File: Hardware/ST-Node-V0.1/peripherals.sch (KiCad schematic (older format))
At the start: 30 parts, among them Q2 2SC4213, SW2 SW_Push, U10 LIS2DH12, U11 SHTC3, U12 ATECC608A-TNGLORAU, U9 MX25R1635

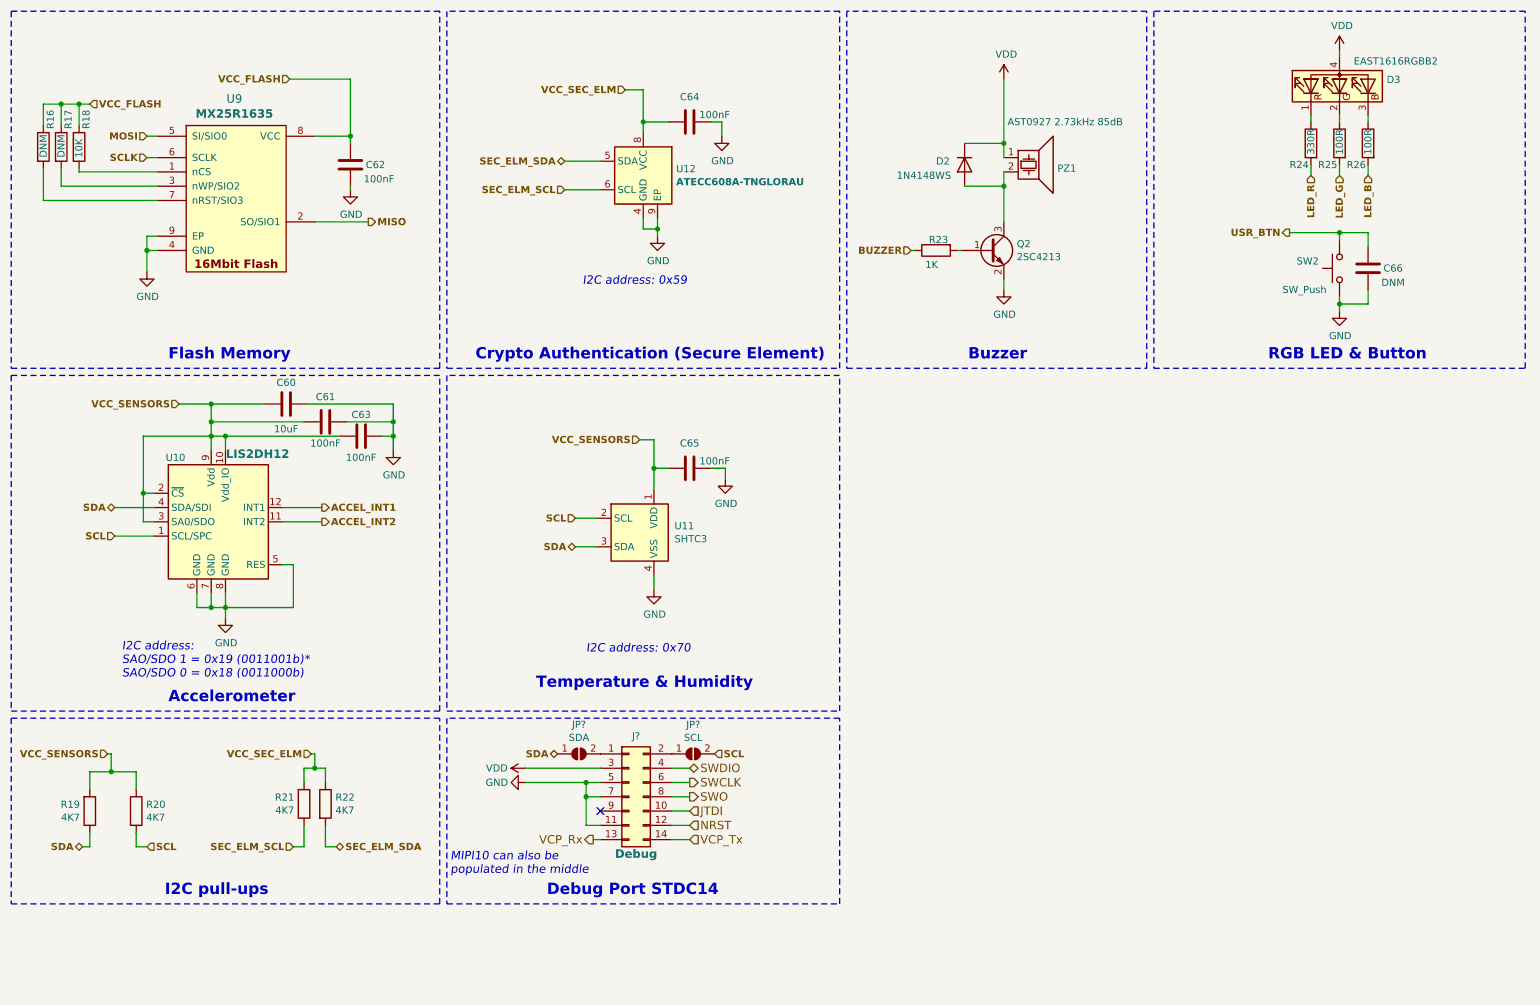
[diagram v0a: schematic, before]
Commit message: sch:  Swap couple of pins and fix a HW bug
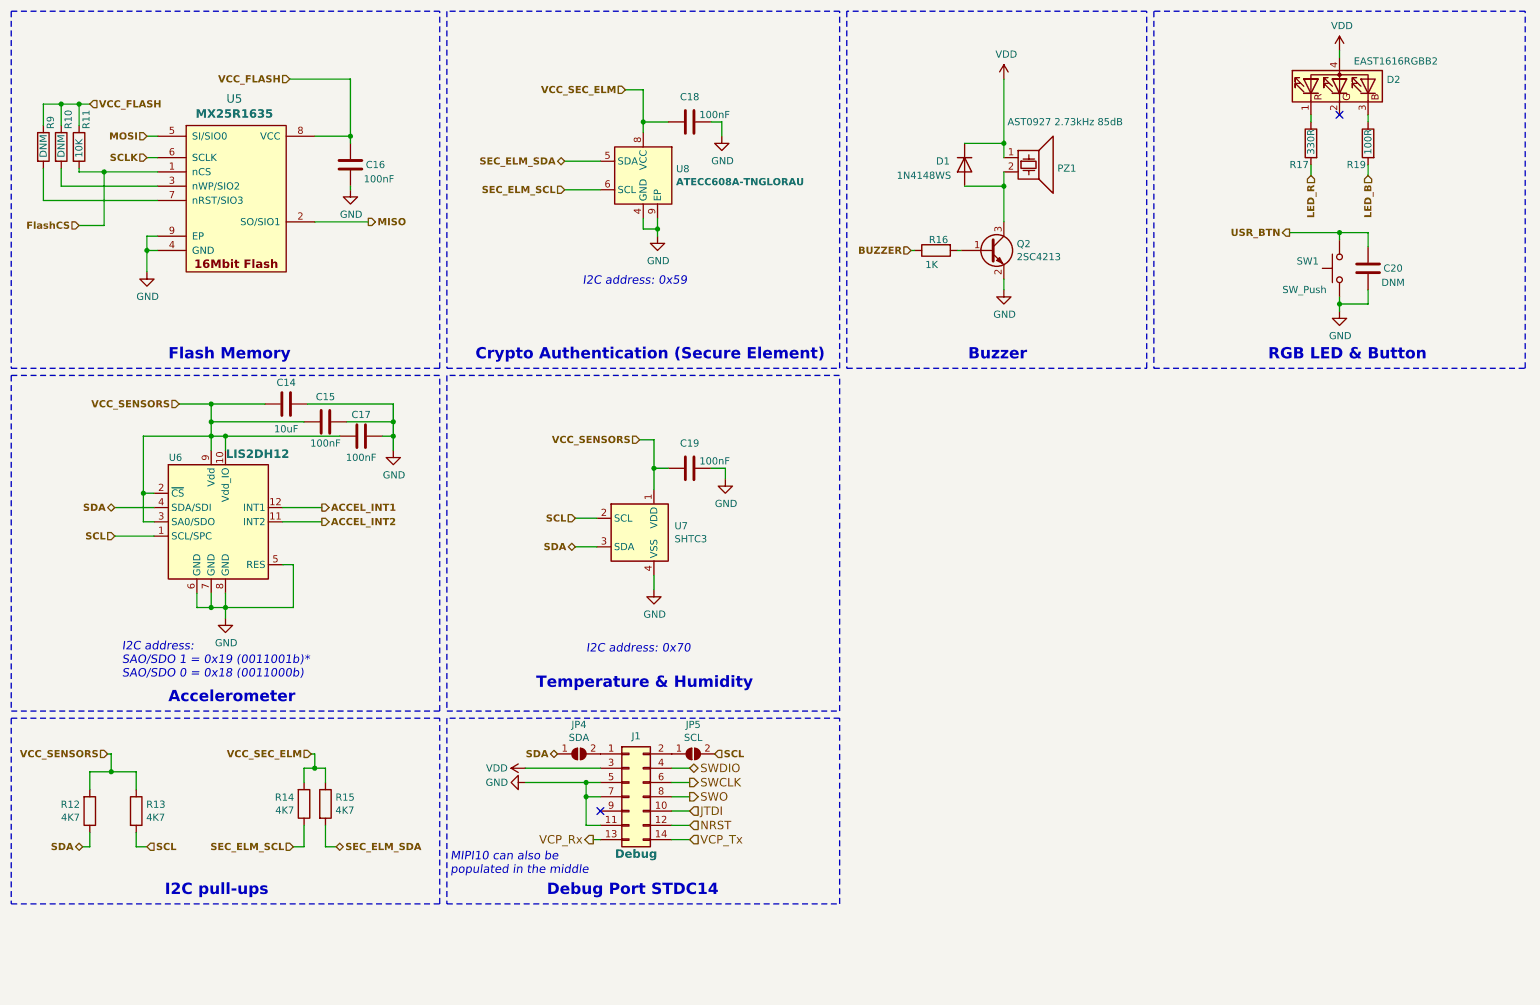
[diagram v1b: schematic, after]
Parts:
- removed R25: 100R, Resistor_SMD:R_0402_1005Metric, symbol Device:R
- J1: renamed from J?; footprint (none) -> Connector_PinHeader_1.27mm:PinHeader_2x07_P1.27mm_Vertical_SMD
- JP4, JP5: renamed from JP?; footprint (none) -> Jumper:SolderJumper-2_P1.3mm_Open_RoundedPad1.0x1.5mm
- renumbered C60 to C14, C61 to C15, C62 to C16, C63 to C17, C64 to C18, C65 to C19, C66 to C20, D2 to D1, D3 to D2, R17 to R10, R18 to R11, R19 to R12, R20 to R13, R21 to R14, R22 to R15, R23 to R16, R24 to R17, R26 to R19, R16 to R9, SW2 to SW1, U9 to U5, U10 to U6, U11 to U7, U12 to U8
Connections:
- net FlashCS: now reaches R11.2, U5.1 (nCS)
- no-connect marks 1 -> 2

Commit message: sch, pcb: Improve pcb layout, swap sch pins
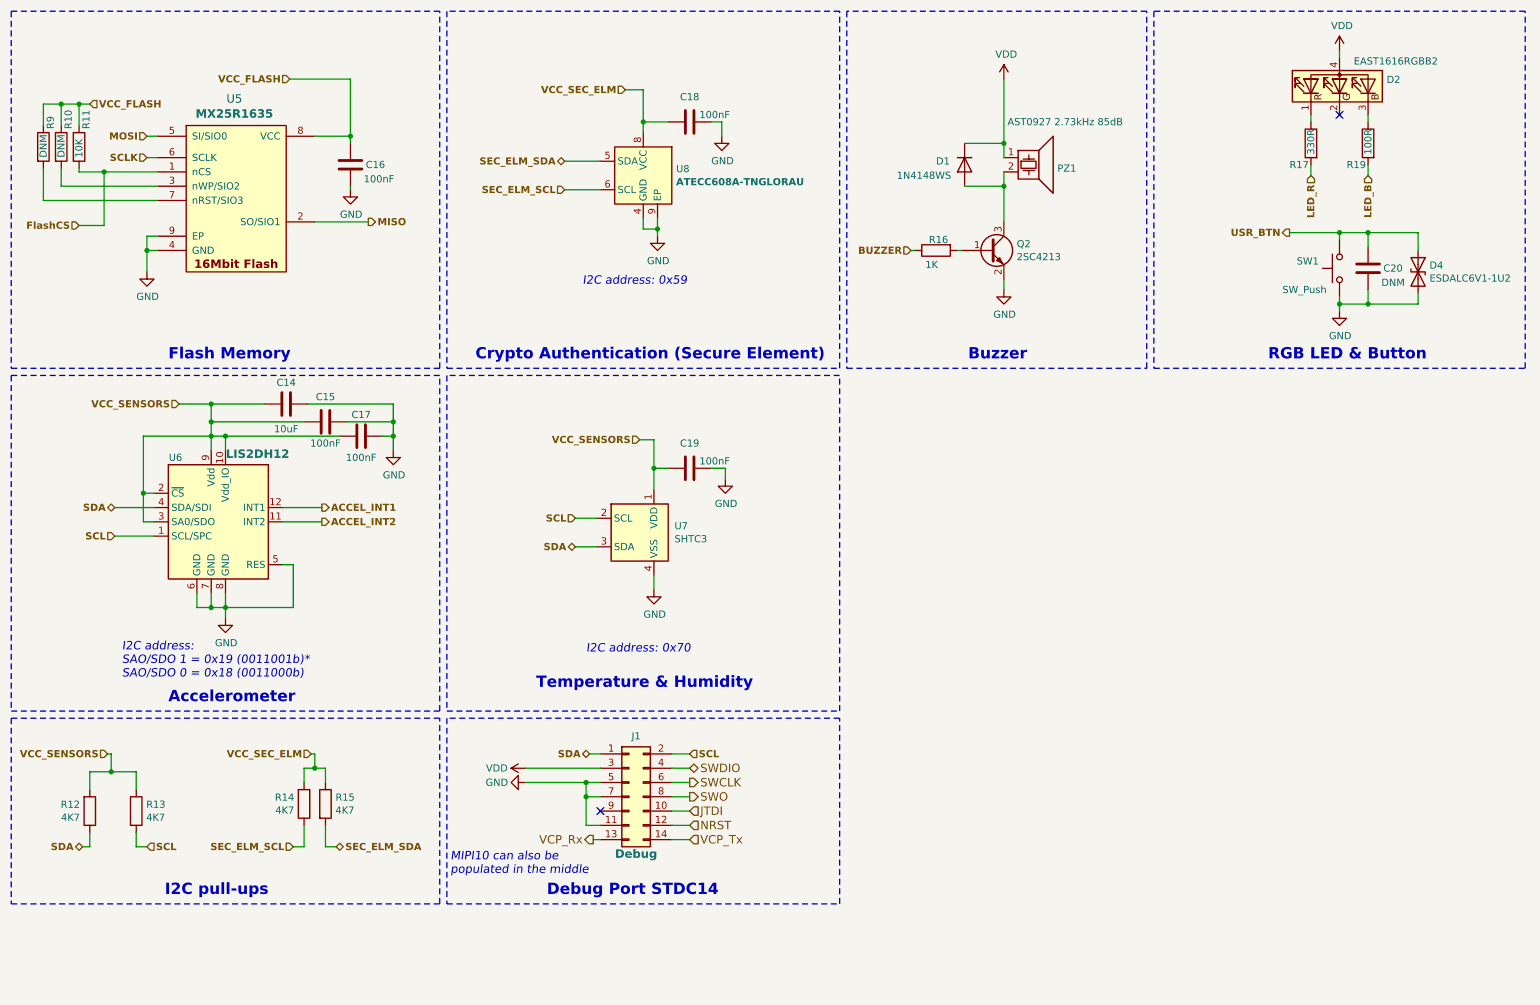
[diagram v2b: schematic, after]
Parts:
- removed JP4: SDA, Jumper:SolderJumper-2_P1.3mm_Open_RoundedPad1.0x1.5mm, symbol Jumper:SolderJumper_2_Open
- removed JP5: SCL, Jumper:SolderJumper-2_P1.3mm_Open_RoundedPad1.0x1.5mm, symbol Jumper:SolderJumper_2_Open
- added D4: ESDALC6V1-1U2, Diode_SMD:D_0201_0603Metric, symbol Device:D_TVS
- C14: MPN (none) -> C1608X5R0J106K080AB
- C15, C16, C17, C18, C19: MPN (none) -> CC0402KRX7R7BB104
- D2: footprint LED_SMD:LED_RGB_1210 -> node-lib-v1:LED_RGB_0606
- J1: footprint Connector_PinHeader_1.27mm:PinHeader_2x07_P1.27mm_Vertical_SMD -> node-lib-v1:PinHeader_2x07_P1.27mm_Vertical_SMD; MPN (none) -> FTSH-107-01-F-DV-K
- PZ1: footprint Buzzer_Beeper:MagneticBuzzer_CUI_CST-931RP-A -> node-lib-v1:Buzzer_AST0927MW-3.6TRQ
- R10, R9: MPN (none) -> DNM
- R11: MPN (none) -> AC0402JR-0710KL
- R12, R13, R14, R15: MPN (none) -> AC0402FR-074K7L
- R16: MPN (none) -> RC0402FR-071KP
- R17: MPN (none) -> AC0402FR-07330RL
- R19: MPN (none) -> RC0402FR-07100RL
- SW1: footprint Button_Switch_SMD:SW_SPST_B3S-1000 -> node-lib-v1:EVQ-P2R02W; MPN KMR211GLFS -> EVQ-P2R02W
- U5: footprint Package_CSP:LFCSP-8-1EP_3x2mm_P0.5mm_EP1.6x1.65mm -> node-lib-v1:FLASH_UFDFN-8-MX25R1635F
- U7: footprint Sensor_Humidity:Sensirion_DFN-4-1EP_2x2mm_P1mm_EP0.7x1.6mm -> node-lib-v1:Sensirion_DFN-4-1EP_2x2mm_P1mm_EP0.7x1.6mm; MPN (none) -> SHTC3
- U8: MPN ATECC608A-TNGLORAU-G -> ATECC608A-TNGLORAU-B
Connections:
- net GND: now also D4.2 (A2)
- net SCL: now also J1.2 (Pin_2)
- net SDA: now also J1.1 (Pin_1)
- net USR_BTN: now also D4.1 (A1)
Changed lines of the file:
@@
 F 0 "U5" H 2112 1687 59  0000 C CNN
 F 1 "MX25R1635" H 2112 1582 59  0000 C CNB
-F 2 "Package_CSP:LFCSP-8-1EP_3x2mm_P0.5mm_EP1.6x1.65mm" H 1775 1425 59  0001 C CNN
+F 2 "node-lib-v1:FLASH_UFDFN-8-MX25R1635F" H 1775 1425 59  0001 C CNN
 F 3 "" H 1775 1425 59  0001 C CNN
 F 4 "MX25R1635FZUIL0" H 1775 1425 50  0001 C CNN "MPN"
@@
 F 2 "Capacitor_SMD:C_0603_1608Metric" H 2513 3150 50  0001 C CNN
 F 3 "~" H 2475 3300 50  0001 C CNN
+F 4 "C1608X5R0J106K080AB" V 2475 3300 50  0001 C CNN "MPN"
 	1    2475 3300
 	0    1    1    0
@@
 F 2 "Capacitor_SMD:C_0402_1005Metric" H 2788 3275 50  0001 C CNN
 F 3 "~" H 2750 3425 50  0001 C CNN
+F 4 "CC0402KRX7R7BB104" H 2750 3425 50  0001 C CNN "MPN"
 	1    2750 3425
 	0    1    1    0
@@
 F 2 "Capacitor_SMD:C_0402_1005Metric" H 3038 3375 50  0001 C CNN
 F 3 "~" H 3000 3525 50  0001 C CNN
+F 4 "CC0402KRX7R7BB104" H 3000 3525 50  0001 C CNN "MPN"
 	1    3000 3525
 	0    1    1    0
@@
 F 2 "Capacitor_SMD:C_0402_1005Metric" H 2963 1475 50  0001 C CNN
 F 3 "~" H 2925 1625 50  0001 C CNN
+F 4 "CC0402KRX7R7BB104" H 2925 1625 50  0001 C CNN "MPN"
 	1    2925 1625
 	-1   0    0    1
@@
 	1575 1575 1500 1575
 $Comp
-L Device:R R11
-U 1 1 5EBDE849
-P 1025 1500
-F 0 "R11" V 1075 1625 50  0000 L CNN
-F 1 "10K" V 1025 1425 50  0000 L CNN
-F 2 "Resistor_SMD:R_0402_1005Metric" V 955 1500 50  0001 C CNN
-F 3 "~" H 1025 1500 50  0001 C CNN
-	1    1025 1500
-	1    0    0    -1
-$EndComp
-$Comp
 L Device:R R10
 U 1 1 5EBDF77C
@@
 F 2 "Resistor_SMD:R_0402_1005Metric" V 830 1500 50  0001 C CNN
 F 3 "~" H 900 1500 50  0001 C CNN
+F 4 "DNM" H 900 1500 50  0001 C CNN "MPN"
 	1    900  1500
 	1    0    0    -1
@@
 F 2 "Resistor_SMD:R_0402_1005Metric" V 705 1500 50  0001 C CNN
 F 3 "~" H 775 1500 50  0001 C CNN
+F 4 "DNM" H 775 1500 50  0001 C CNN "MPN"
 	1    775  1500
 	1    0    0    -1
@@
 F 2 "Capacitor_SMD:C_0402_1005Metric" H 5338 1175 50  0001 C CNN
 F 3 "~" H 5300 1325 50  0001 C CNN
+F 4 "CC0402KRX7R7BB104" H 5300 1325 50  0001 C CNN "MPN"
 	1    5300 1325
 	0    1    1    0
@@
 F 2 "Package_DFN_QFN:DFN-8-1EP_3x2mm_P0.5mm_EP1.3x1.5mm" H 4975 1700 50  0001 C CNN
 F 3 "http://ww1.microchip.com/downloads/en/DeviceDoc/ATECC608A-CryptoAuthentication-Device-Summary-Data-Sheet-DS40001977B.pdf" H 5125 1950 50  0001 C CNN
-F 4 "ATECC608A-TNGLORAU-G" H 4975 1700 50  0001 C CNN "MPN"
+F 4 "ATECC608A-TNGLORAU-B" H 4975 1700 50  0001 C CNN "MPN"
 	1    4975 1700
 	-1   0    0    -1
@@
 F 0 "PZ1" H 7875 1500 50  0000 L CNN
 F 1 "AST0927 2.73kHz 85dB" H 7525 1825 50  0000 L CNN
-F 2 "Buzzer_Beeper:MagneticBuzzer_CUI_CST-931RP-A" H 7665 1525 50  0001 C CNN
+F 2 "node-lib-v1:Buzzer_AST0927MW-3.6TRQ" H 7665 1525 50  0001 C CNN
 F 3 "~" H 7665 1525 50  0001 C CNN
 F 4 "AST0927MW-3.6TRQ" H 7700 1575 50  0001 C CNN "MPN"
@@
 F 2 "Resistor_SMD:R_0402_1005Metric" V 6955 2225 50  0001 C CNN
 F 3 "~" H 7025 2225 50  0001 C CNN
+F 4 "RC0402FR-071KP" H 7025 2225 50  0001 C CNN "MPN"
 	1    7025 2225
 	0    -1   1    0
@@
 F 0 "D2" V 9896 745 50  0000 R CNN
 F 1 "EAST1616RGBB2" V 10025 975 50  0000 R CNN
-F 2 "LED_SMD:LED_RGB_1210" H 9850 1025 50  0001 C CNN
+F 2 "node-lib-v1:LED_RGB_0606" H 9850 1025 50  0001 C CNN
 F 3 "~" H 9850 1025 50  0001 C CNN
 F 4 "EAST1616RGBB2" V 9850 1075 50  0001 C CNN "MPN"
@@
 F 2 "Resistor_SMD:R_0402_1005Metric" V 9580 1475 50  0001 C CNN
 F 3 "~" H 9650 1475 50  0001 C CNN
+F 4 "AC0402FR-07330RL" H 9650 1475 50  0001 C CNN "MPN"
 	1    9650 1475
 	-1   0    0    -1
@@
 F 2 "Resistor_SMD:R_0402_1005Metric" V 9980 1475 50  0001 C CNN
 F 3 "~" H 10050 1475 50  0001 C CNN
+F 4 "RC0402FR-07100RL" H 10050 1475 50  0001 C CNN "MPN"
 	1    10050 1475
 	-1   0    0    -1
@@
 F 0 "SW1" V 9900 2650 50  0000 R CNN
 F 1 "SW_Push" V 9700 2750 50  0000 R CNN
-F 2 "Button_Switch_SMD:SW_SPST_B3S-1000" H 9850 2550 50  0001 C CNN
+F 2 "node-lib-v1:EVQ-P2R02W" H 9850 2550 50  0001 C CNN
 F 3 "~" H 9850 2550 50  0001 C CNN
-F 4 "KMR211GLFS" H 9850 2350 50  0001 C CNN "MPN"
+F 4 "EVQ-P2R02W" H 9850 2350 50  0001 C CNN "MPN"
 	1    9850 2350
 	0    -1   -1   0
@@
 F 0 "U7" H 5194 4246 50  0000 L CNN
 F 1 "SHTC3" H 5194 4155 50  0000 L CNN
-F 2 "Sensor_Humidity:Sensirion_DFN-4-1EP_2x2mm_P1mm_EP0.7x1.6mm" H 5150 3850 50  0001 C CNN
+F 2 "node-lib-v1:Sensirion_DFN-4-1EP_2x2mm_P1mm_EP0.7x1.6mm" H 5150 3850 50  0001 C CNN
 F 3 "https://www.sensirion.com/fileadmin/user_upload/customers/sensirion/Dokumente/0_Datasheets/Humidity/Sensirion_Humidity_Sensors_SHTC3_Datasheet.pdf" H 4650 4650 50  0001 C CNN
+F 4 "SHTC3" H 4950 4200 50  0001 C CNN "MPN"
 	1    4950 4200
 	1    0    0    -1
@@
 F 2 "Capacitor_SMD:C_0402_1005Metric" H 5338 3600 50  0001 C CNN
 F 3 "~" H 5300 3750 50  0001 C CNN
+F 4 "CC0402KRX7R7BB104" H 5300 3750 50  0001 C CNN "MPN"
 	1    5300 3750
 	0    1    1    0
@@
 F 2 "Resistor_SMD:R_0402_1005Metric" V 2680 6100 50  0001 C CNN
 F 3 "~" H 2750 6100 50  0001 C CNN
+F 4 "AC0402FR-074K7L" H 2750 6100 50  0001 C CNN "MPN"
 	1    2750 6100
 	1    0    0    -1
@@
 F 2 "Resistor_SMD:R_0402_1005Metric" V 2530 6100 50  0001 C CNN
 F 3 "~" H 2600 6100 50  0001 C CNN
+F 4 "AC0402FR-074K7L" H 2600 6100 50  0001 C CNN "MPN"
 	1    2600 6100
 	1    0    0    1
@@
 F 2 "Resistor_SMD:R_0402_1005Metric" V 1355 6150 50  0001 C CNN
 F 3 "~" H 1425 6150 50  0001 C CNN
+F 4 "AC0402FR-074K7L" H 1425 6150 50  0001 C CNN "MPN"
 	1    1425 6150
 	1    0    0    -1
@@
 F 2 "Resistor_SMD:R_0402_1005Metric" V 1030 6150 50  0001 C CNN
 F 3 "~" H 1100 6150 50  0001 C CNN
+F 4 "AC0402FR-074K7L" H 1100 6150 50  0001 C CNN "MPN"
 	1    1100 6150
 	1    0    0    1
@@
 F 0 "J1" H 4925 6475 50  0000 C CNN
 F 1 "Debug" H 4925 5650 59  0000 C CNB
-F 2 "Connector_PinHeader_1.27mm:PinHeader_2x07_P1.27mm_Vertical_SMD" H 4875 6050 50  0001 C CNN
+F 2 "node-lib-v1:PinHeader_2x07_P1.27mm_Vertical_SMD" H 4875 6050 50  0001 C CNN
 F 3 "~" H 4875 6050 50  0001 C CNN
+F 4 "FTSH-107-01-F-DV-K" H 4875 6050 50  0001 C CNN "MPN"
 	1    4875 6050
 	1    0    0    -1
@@
 Text Notes 4300 6750 0    79   ~ 16
 Debug Port STDC14
-Text HLabel 4375 5750 0    50   BiDi ~ 10
+Text HLabel 4600 5750 0    50   BiDi ~ 10
 SDA
 Wire Wire Line
 	4150 5850 4675 5850
-$Comp
-L Jumper:SolderJumper_2_Open JP4
-U 1 1 5EFF1990
-P 4525 5750
-F 0 "JP4" H 4525 5955 50  0000 C CNN
-F 1 "SDA" H 4525 5864 50  0000 C CNN
-F 2 "Jumper:SolderJumper-2_P1.3mm_Open_RoundedPad1.0x1.5mm" H 4525 5750 50  0001 C CNN
-F 3 "~" H 4525 5750 50  0001 C CNN
-	1    4525 5750
-	1    0    0    -1
-$EndComp
-$Comp
-L Jumper:SolderJumper_2_Open JP5
-U 1 1 5EFF272E
-P 5325 5750
-F 0 "JP5" H 5325 5955 50  0000 C CNN
-F 1 "SCL" H 5325 5864 50  0000 C CNN
-F 2 "Jumper:SolderJumper-2_P1.3mm_Open_RoundedPad1.0x1.5mm" H 5325 5750 50  0001 C CNN
-F 3 "~" H 5325 5750 50  0001 C CNN
-	1    5325 5750
-	1    0    0    -1
-$EndComp
-Text HLabel 5475 5750 2    50   Input ~ 10
+Text HLabel 5300 5750 2    50   Input ~ 10
 SCL
 Text HLabel 1025 2050 0    50   Input ~ 10
@@
 	1200 1675 1575 1675
 NoConn ~ 9850 1275
+$Comp
+L Device:R R11
+U 1 1 5EBDE849
+P 1025 1500
+F 0 "R11" V 1075 1625 50  0000 L CNN
+F 1 "10K" V 1025 1425 50  0000 L CNN
+F 2 "Resistor_SMD:R_0402_1005Metric" V 955 1500 50  0001 C CNN
+F 3 "~" H 1025 1500 50  0001 C CNN
+F 4 "AC0402JR-0710KL" H 1025 1500 50  0001 C CNN "MPN"
+	1    1025 1500
+	1    0    0    -1
+$EndComp
+$Comp
+L Device:D_TVS D?
+U 1 1 5EEDF63C
+P 10400 2375
+AR Path="/5EA70AC3/5EEDF63C" Ref="D?"  Part="1"
+AR Path="/5EB1DE63/5EEDF63C" Ref="D4"  Part="1"
+F 0 "D4" V 10354 2455 50  0000 L CNN
+F 1 "ESDALC6V1-1U2" V 10445 2455 50  0000 L CNN
+F 2 "Diode_SMD:D_0201_0603Metric" H 10400 2375 50  0001 C CNN
+F 3 "~" H 10400 2375 50  0001 C CNN
+F 4 "ESDALC6V1-1U2" V 10400 2375 50  0001 C CNN "MPN"
+	1    10400 2375
+	0    1    1    0
+$EndComp
+Wire Wire Line
+	10400 2225 10400 2100
+Wire Wire Line
+	10400 2100 10050 2100
+Connection ~ 10050 2100
+Wire Wire Line
+	10400 2525 10400 2600
+Wire Wire Line
+	10400 2600 10050 2600
+Connection ~ 10050 2600
+Wire Wire Line
+	5300 5750 5175 5750
+Wire Wire Line
+	4600 5750 4675 5750
 $EndSCHEMATC

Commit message: pcb, doc: Add final production files, add interaction PnP iBOM
dev: Add gitignore for KiCAD files


all: Delete unused media files
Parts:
- added J3: Grove_I2C, Connector:NS-Tech_Grove_1x04_P2mm_Vertical, symbol Connector_Generic:Conn_01x04
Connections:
- net GND: now also J3.4 (Pin_4)
- net SCL: now also J3.1 (Pin_1)
- net SDA: now also J3.2 (Pin_2)
- net VCC_SENSORS: now also J3.3 (Pin_3)
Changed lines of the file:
@@
 Wire Wire Line
 	4600 5750 4675 5750
+$Comp
+L Connector_Generic:Conn_01x04 J3
+U 1 1 5EF3C2B8
+P 4925 7175
+F 0 "J3" H 5005 7167 50  0000 L CNN
+F 1 "Grove_I2C" H 5005 7076 50  0000 L CNN
+F 2 "Connector:NS-Tech_Grove_1x04_P2mm_Vertical" H 4925 7175 50  0001 C CNN
+F 3 "~" H 4925 7175 50  0001 C CNN
+	1    4925 7175
+	1    0    0    -1
+$EndComp
+Text HLabel 4650 7175 0    50   BiDi ~ 10
+SDA
+Text HLabel 4650 7075 0    50   Input ~ 10
+SCL
+Text HLabel 4650 7275 0    50   Input ~ 10
+VCC_SENSORS
+$Comp
+L power:GND #PWR091
+U 1 1 5EF3D9FD
+P 4650 7375
+F 0 "#PWR091" H 4650 7125 50  0001 C CNN
+F 1 "GND" V 4650 7175 50  0000 C CNN
+F 2 "" H 4650 7375 50  0001 C CNN
+F 3 "" H 4650 7375 50  0001 C CNN
+	1    4650 7375
+	0    1    1    0
+$EndComp
+Wire Wire Line
+	4725 7375 4650 7375
+Wire Wire Line
+	4650 7275 4725 7275
+Wire Wire Line
+	4650 7175 4725 7175
+Wire Wire Line
+	4650 7075 4725 7075
 $EndSCHEMATC
